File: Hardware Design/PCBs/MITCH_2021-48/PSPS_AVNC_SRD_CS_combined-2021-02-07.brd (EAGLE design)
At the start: 8 parts, among them IC1 74HC595LSFK, IC2 74HC595LSFK, U0-C STM32F411CEUX

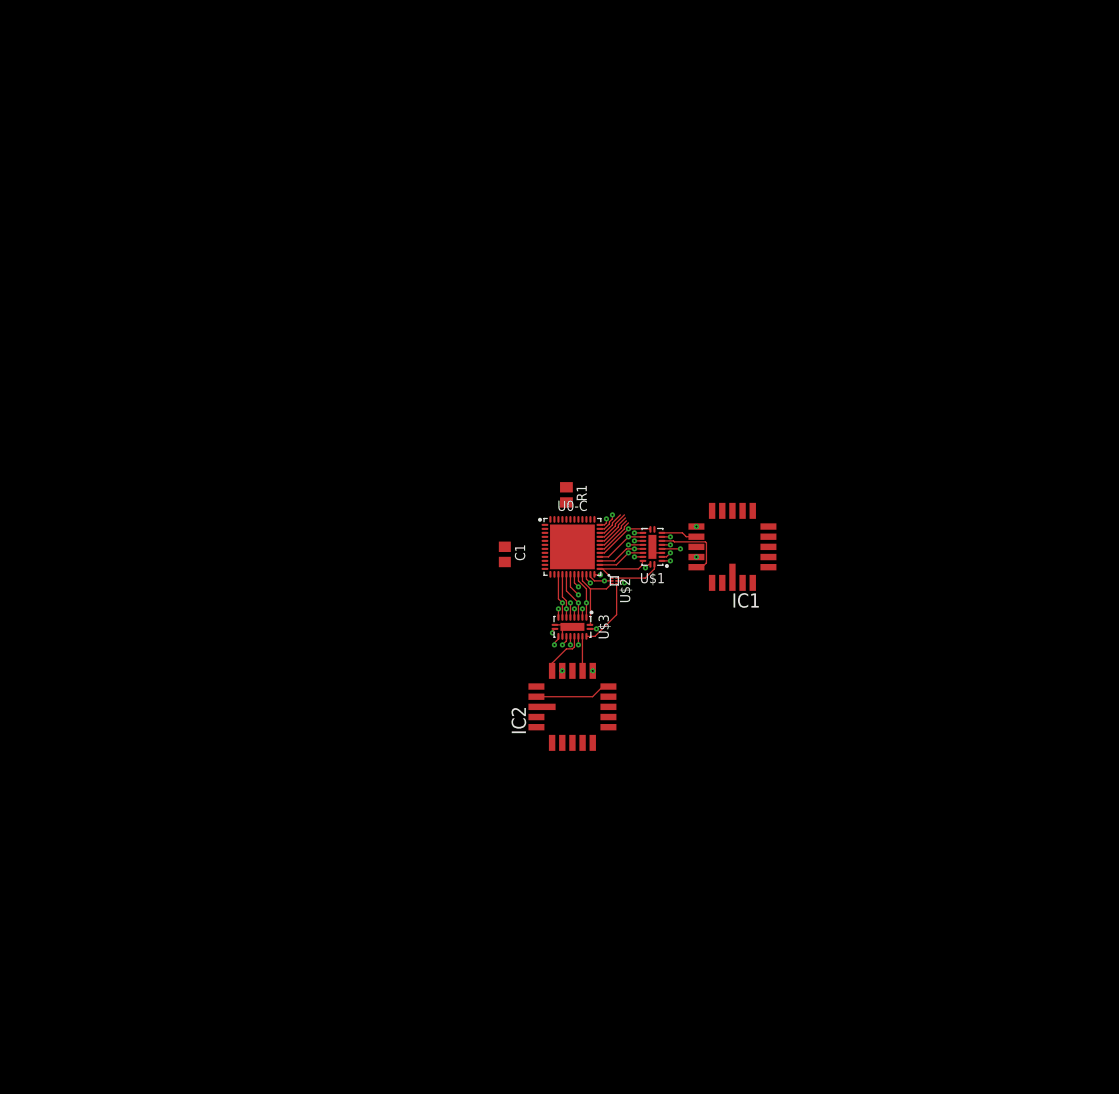
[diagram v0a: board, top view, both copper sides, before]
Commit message: Replaces shift registers with dual quad
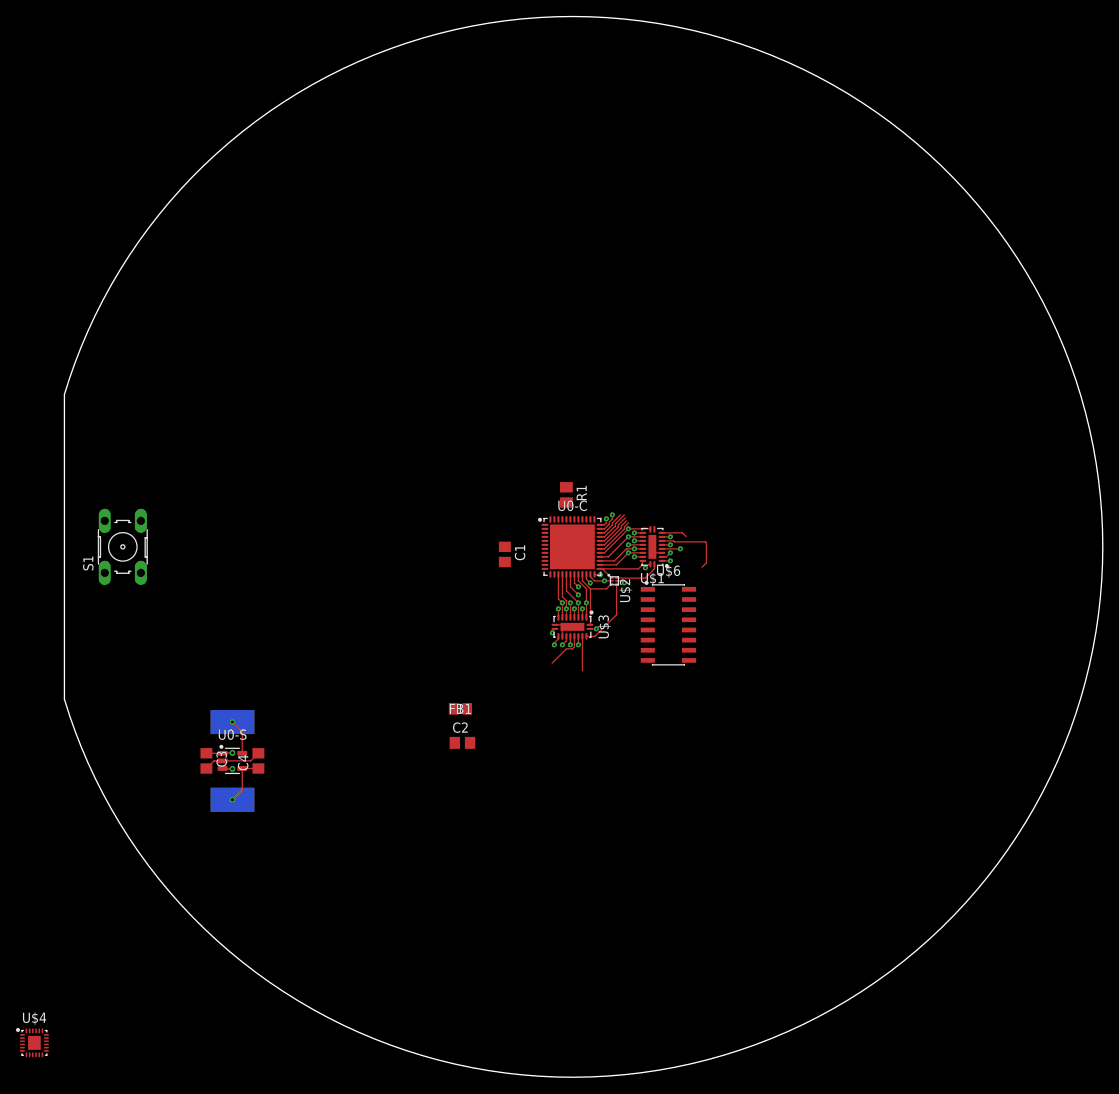
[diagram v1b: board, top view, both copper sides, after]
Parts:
- removed IC1, IC2: 74HC595LSFK, Computer2:LCC20
- added C2: 0.1 uF, resistor:C0805
- added C3, C4: 4.7 uF, resistor:C0805
- added FB1: MMZ2012Y152B, Computer2:BEADC2012X105N
- added S1: (no value), switch-omron:B3F-10XX
- added U$4: ICM-20948, Computer2:QFN40P300X300X105-25T159X175
- added U$5: L-US5050, Computer2:INDDFN1250X1250X600-2N
- added U$6: HEF4015B, Computer2:SOIC127P600X265-16N
- added U0-S: TPS62202, Computer2:SOT95P280X145-5
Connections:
- removed net SPI1_CS0: IC2.19
- removed net SPI1_CS1: IC2.2
- removed net SPI1_CS2: IC2.3
- removed net SPI1_CS3: IC2.4
- removed net SPI1_CS4: IC2.5
- removed net SPI1_CS5: IC2.7
- removed net SPI1_CS6: IC2.8
- removed net SPI1_CS7: IC2.9
- removed net SPI2_CS0: IC1.19
- removed net SPI2_CS1: IC1.2
- removed net SPI2_CS2: IC1.3
- removed net SPI2_CS3: IC1.4
- removed net SPI2_CS4: IC1.5
- removed net SPI2_CS5: IC1.7
- removed net SPI2_CS6: IC1.8
- removed net SPI2_CS7: IC1.9
- new net 1V8: C4.1, U$5.2, U0-S.4
- new net U0-S_SW: U$5.1, U0-S.5
- net 3V3: now also C3.1, FB1.2, U0-S.1, U0-S.3; no longer IC1.13, IC1.20, IC2.13, IC2.20
- net GND: now also C2.2, C3.2, C4.2, S1.3, S1.4, U$6.8, U0-S.2; no longer IC1.10, IC1.17, IC2.10, IC2.17
- net NRST: now also C2.1, S1.1, S1.2
- net SPI1R_LE: no longer IC2.15
- net SPI1R_MOSI: no longer IC2.18
- net SPI1R_SCK: no longer IC2.14
- net SPI2R_LE: no longer IC1.15
- net SPI2R_MOSI: no longer IC1.18
- net SPI2R_SCK: no longer IC1.14
- net VDDA: now also FB1.1
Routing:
- net GND: track 11.9 -> 19.2 mm, vias 4 -> 2
- net 1V8: track 0.00 -> 6.43 mm, vias 0 -> 1
- net 3V3: track 14.4 -> 9.42 mm, vias 5 -> 7
- net U0-S_SW: track 0.00 -> 4.41 mm, vias 0 -> 1
- net SPI2R_LE: track 4.51 -> 3.24 mm
- net SPI1R_MOSI: track 5.91 -> 4.95 mm
- net SPI2R_MOSI: track 9.64 -> 8.93 mm
- net SPI2R_SCK: vias 2 -> 1
- net SPI1R_SCK: vias 2 -> 1
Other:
- board outline added: 129.8 x 132.6 mm

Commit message: Update to PCB
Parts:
- added C5, C6, C7, C8: 0.1 uF, resistor:C0805
- added U$10, U$7, U$8, U$9: SN74LV1T34, Computer2:SOT65P210X110-5
- added U$11: MS5607, Computer2:MS5607
- added U1-S: ICM-20948, Computer2:QFN40P300X300X105-25T159X175
- U$2: value 74LVC2G14 -> 74LVC2G14TSOP; device Computer2:SOT1202 -> Computer2:SOP95P280X110-6N
- U$4: value ICM-20948 -> 74ALVC08; device Computer2:QFN40P300X300X105-25T159X175 -> Computer2:QFN50P300X250X100-15T150X100N
- moved U$4 99.3 mm to (18.0, -11.0)
- moved C2 45.2 mm to (-51.8, 0.00), turned to 90 degrees
- moved FB1 21.6 mm to (-5.75, -0.25), turned to 90 degrees
- moved C1 14.6 mm to (4.50, -7.75)
- moved U$6 2.36 mm to (10.0, -11.0)
- moved U$2 1.50 mm to (6.75, -4.25), turned to 0 degrees
- moved R1 1.06 mm to (-1.50, 5.75), turned to 0 degrees
- turned S1 to 270 degrees
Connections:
- new net CS_1V8: U$9.4, U1-S.22
- new net MISO_1V8: U$10.2, U1-S.9
- new net MOSI_1V8: U$7.4, U1-S.24
- new net SCK_1V8: U$8.4, U1-S.23
- new net SPI1_CS0: U$6.5
- new net SPI1_CS1: U$6.4, U$9.2
- new net SPI1_CS2: U$11.P$5, U$6.3
- new net SPI1_CS3: U$6.2
- new net SPI2_CS0: U$4.13, U$6.13
- new net SPI2_CS1: U$4.2, U$6.12
- new net SPI2_CS2: U$4.4, U$6.11
- new net SPI2_CS3: U$4.9, U$6.10
- new net SPI2_SCK0: U$4.11
- new net SPI2_SCK1: U$4.3
- new net SPI2_SCK2: U$4.6
- new net SPI2_SCK3: U$4.8
- new net U1-S_REGOUT: C5.1, U1-S.10
- net !SPI1_REG!: now also U$2.4; no longer U$2.P4
- net !SPI2_REG!: now also U$2.6; no longer U$2.P6
- net 1V8: now also C6.1, C7.1, U$7.5, U$8.5, U$9.5, U1-S.13, U1-S.8
- net 3V3: now also C8.1, U$10.5, U$11.P$1, U$2.5, U$4.14, U$6.16; no longer U$2.P5
- net GND: now also C5.2, C6.2, C7.2, C8.2, U$10.3, U$11.P$2, U$11.P$3, U$2.2, U$4.15, U$4.7, U$7.3, U$8.3, U$9.3, U1-S.18, U1-S.20; no longer U$2.P2
- net NRST: no longer S1.1
- net SPI1B_MISO: now also U$10.4, U$11.P$6
- net SPI1B_MOSI: now also U$11.P$7, U$7.2
- net SPI1B_SCK: now also U$11.P$8, U$8.2
- net SPI1R_LE: now also U$6.6
- net SPI1R_MOSI: now also U$6.7
- net SPI1R_SCK: now also U$6.1
- net SPI1_REG: now also U$2.3; no longer U$2.P3
- net SPI2R_LE: now also U$6.14
- net SPI2R_MOSI: now also U$6.15
- net SPI2R_SCK: now also U$6.9
- net SPI2_REG: now also U$2.1; no longer U$2.P1
- net SPI2_SCK: now also U$4.1, U$4.10, U$4.12, U$4.5
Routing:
- net GND: track 19.2 -> 117.2 mm, vias 2 -> 13
- net 3V3: track 9.42 -> 68.0 mm, vias 7 -> 13
- net NRST: track 0.00 -> 52.0 mm
- net 1V8: track 6.43 -> 38.3 mm, vias 1 -> 5
- net SPI2_SCK: track 12.7 -> 35.9 mm, vias 2 -> 5
- net SPI1B_MOSI: track 1.07 -> 21.0 mm, vias 1 -> 2
- net MISO_1V8: track 0.00 -> 16.9 mm
- net SPI1_CS1: track 0.00 -> 15.0 mm, vias 0 -> 1
- net SPI1B_SCK: track 1.07 -> 15.7 mm, vias 1 -> 2
- net SPI2R_LE: track 3.24 -> 14.0 mm
- net SPI2R_SCK: track 6.79 -> 17.5 mm
- net SPI1_CS3: track 0.00 -> 10.7 mm
- net SPI1B_MISO: track 1.82 -> 12.1 mm, vias 1 -> 2
- net SPI1_CS2: track 0.00 -> 9.61 mm
- net SPI2_CS0: track 0.00 -> 9.22 mm
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- added copper zone on layer 2, net 1V8

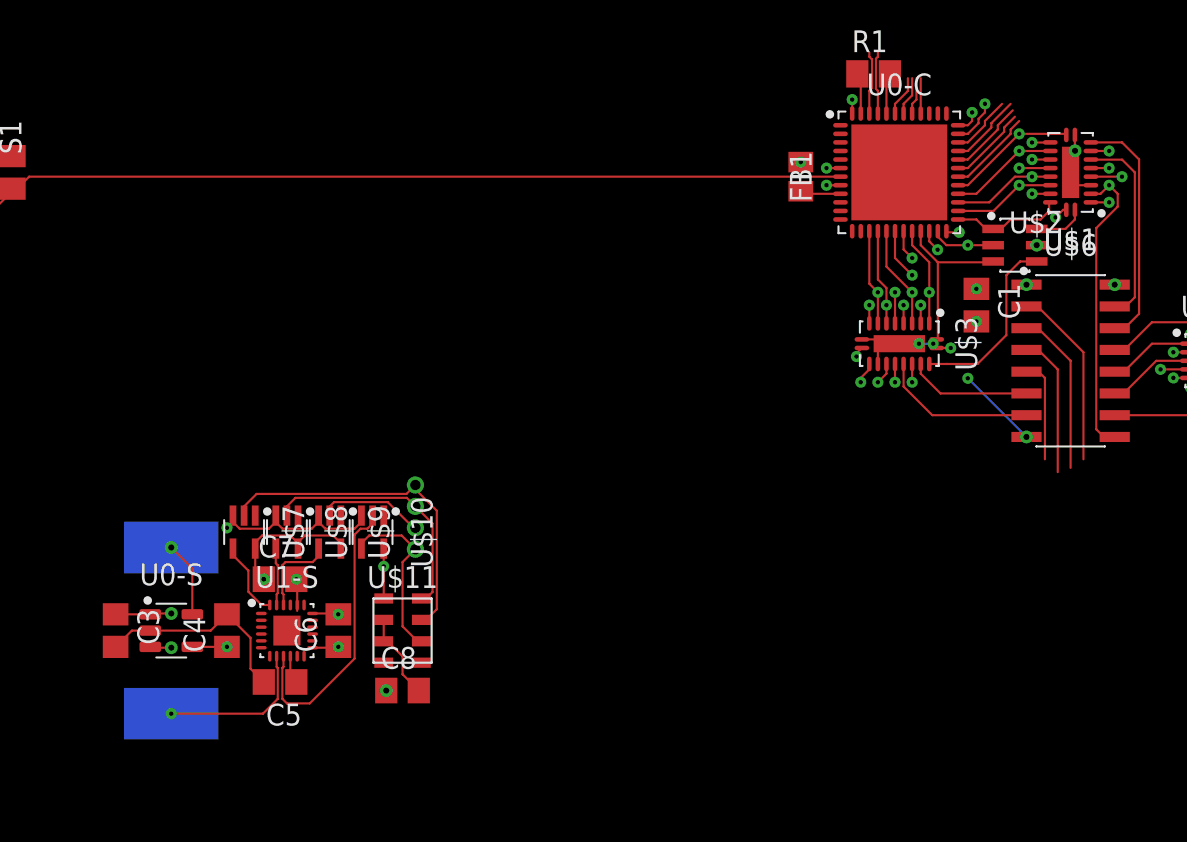
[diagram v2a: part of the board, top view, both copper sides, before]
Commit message: Combined sensor block with processor block
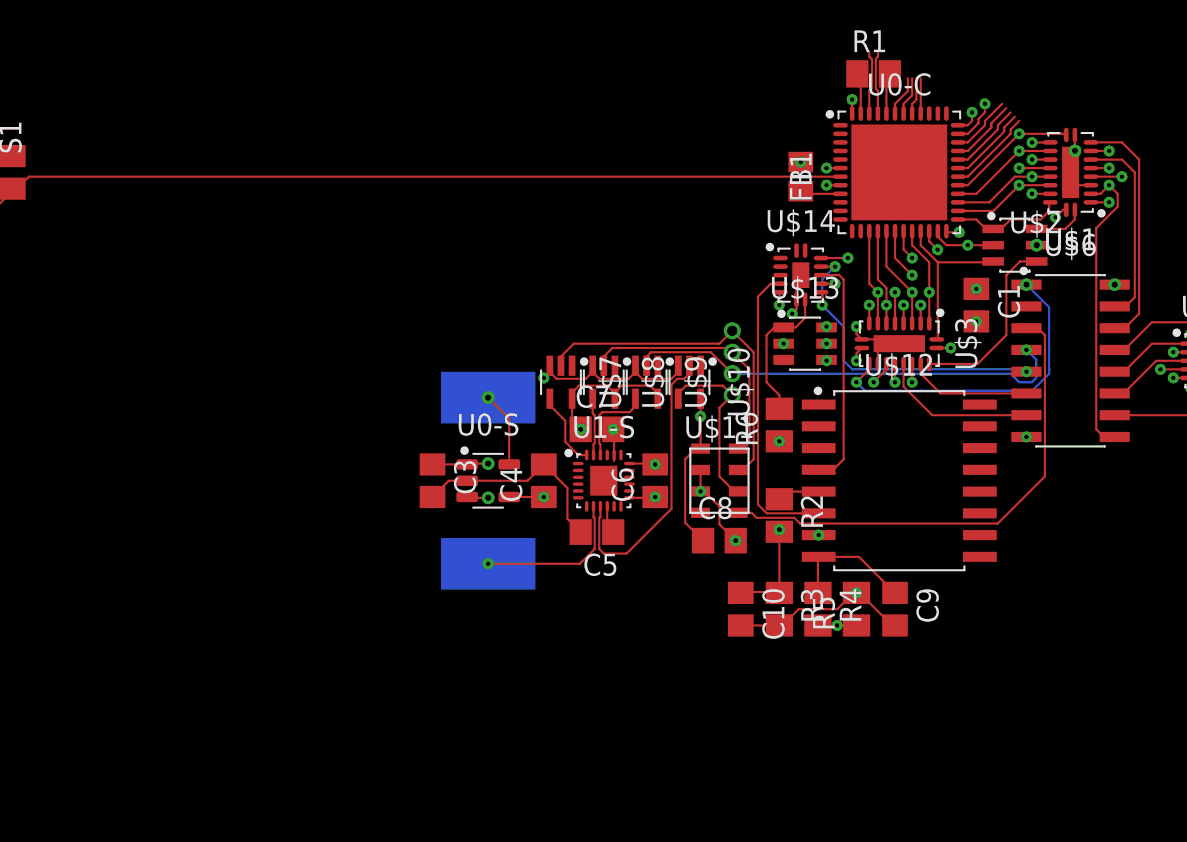
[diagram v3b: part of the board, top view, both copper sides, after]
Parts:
- added C10, C9: 0.1 uF, resistor:C0805
- added R2, R3, R6: 10k, resistor:M0805
- added R4, R5: 100k, resistor:M0805
- added U$12: MMA1211KEG, Computer2:SOIC127P1041X355-16N
- added U$13: TMUX1119, Computer2:SOP95P280X145-6N
- added U$14: 74ALVC08, Computer2:QFN50P300X250X100-15T150X100N
- moved C3 20.5 mm to (-27.2, -18.0)
- moved C4 20.5 mm to (-20.8, -18.0)
- moved C5 20.5 mm to (-17.6, -21.0)
- moved C6 20.5 mm to (-14.2, -18.0)
- moved C7 20.5 mm to (-17.6, -15.0)
- moved C8 20.5 mm to (-10.5, -21.5)
- moved U$10 20.5 mm to (-12.2, -12.2)
- moved U$11 20.5 mm to (-10.5, -18.0)
- moved U$5 20.5 mm to (-24.0, -18.0)
- moved U$7 20.5 mm to (-19.8, -12.2)
- moved U$8 20.5 mm to (-17.2, -12.2)
- moved U$9 20.5 mm to (-14.8, -12.2)
- moved U0-S 20.5 mm to (-24.0, -18.0)
- moved U1-S 20.5 mm to (-17.2, -18.0)
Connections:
- new net 5V: C9.1, R4.1, U$12.8
- new net 5V-MEASURE: R4.2, R5.1, U$13.4
- new net ACCEL_ANALOG_OUT: C10.1, R2.2, R3.1, U$13.6
- new net ACCEL_SEL: R6.2, U$13.1, U$14.8
- new net ST: U$12.4, U$14.11
- new net STATUS: U$12.6, U$14.5
- new net U0-S_VOUT: R2.1, U$12.5
- net 3V3: now also U$13.2, U$14.14
- net ACCEL_ANALOG: now also U$13.5
- net GND: now also C10.2, C9.2, R3.2, R5.2, R6.1, U$12.7, U$13.3, U$14.15, U$14.7
- net SPI1B_LE: now also U$14.10
- net SPI1B_MISO: now also U$14.6
- net SPI1B_MOSI: now also U$14.13
- net SPI1_CS0: now also U$14.12, U$14.9
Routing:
- net GND: track 117.2 -> 179.4 mm, vias 13 -> 18
- net SPI1B_MOSI: track 21.0 -> 48.2 mm, vias 2 -> 3
- net SPI1B_MISO: track 12.1 -> 35.6 mm, vias 2 -> 3
- net SPI1_CS2: track 9.61 -> 28.8 mm
- net ACCEL_ANALOG_OUT: track 0.00 -> 18.9 mm, vias 0 -> 3
- net 5V-MEASURE: track 0.00 -> 18.0 mm, vias 0 -> 2
- net STATUS: track 0.00 -> 17.5 mm
- net ST: track 0.00 -> 13.6 mm
- net SPI1_CS0: track 5.98 -> 19.6 mm, vias 0 -> 3
- net SPI1_CS1: track 15.0 -> 27.2 mm, vias 1 -> 2
- net SPI1B_SCK: track 15.7 -> 26.0 mm
- net SPI1_CS3: track 10.7 -> 0.65 mm
- net ACCEL_ANALOG: track 1.77 -> 10.5 mm, vias 1 -> 2
- net ACCEL_SEL: track 0.00 -> 8.34 mm
- net 3V3: track 68.0 -> 75.6 mm
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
